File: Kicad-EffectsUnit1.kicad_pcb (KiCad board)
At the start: 2 copper layers, 100 x 100 mm, 161 parts, among them J101 In7, J102 Doepfer connector, J104 In6, J105 In3, J106 Out10, J107 Out11, J108 Out9, J109 Out6, J201 In, J202 Out, P201 HEADER_2x5_Doepfer, Q201 BC337, Q202 PZT2222A, Q203 PZT2222A, SW101 Dist 6, SW102 Crush A6, SW104 Rotary_Encoder_Switch, SW105 Dist 10, U101 TL072, U102 TL072, U201 TL072, U202 PT2399

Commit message: misc
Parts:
- removed C203, C204, C207, C208, C209: 100n, Capacitor_SMD:C_0805_2012Metric_Pad1.15x1.40mm_HandSolder
- removed C206: 100uF 16v, Capacitor_THT:CP_Radial_D5.0mm_P2.50mm
- removed D203: 1N1007, Diode_SMD:D_SOD-123
- removed U201: TL072, AJ-Dropbox-Kicad:AJ_SO-8_5.3x6.2mm_P1.27mm
- added C301: 100uF 16v, Capacitor_THT:CP_Radial_D5.0mm_P2.50mm, F.Cu at (228.7, 60.8)
- added C302: 100n, Capacitor_SMD:C_0805_2012Metric_Pad1.15x1.40mm_HandSolder, F.Cu at (209.9, 72.8)
- added C303: 100n, Capacitor_SMD:C_0805_2012Metric_Pad1.15x1.40mm_HandSolder, F.Cu at (221.7, 72.5)
- added C304: 100n, Capacitor_SMD:C_0805_2012Metric_Pad1.15x1.40mm_HandSolder, F.Cu at (232.8, 64.5)
- added C305: 100uF 16v, Capacitor_THT:CP_Radial_D5.0mm_P2.50mm, F.Cu at (221.4, 64.0)
- added C306: 100uF 16v, Capacitor_THT:CP_Radial_D5.0mm_P2.50mm, F.Cu at (215.8, 69.6)
- added C307: 100n, Capacitor_SMD:C_0805_2012Metric_Pad1.15x1.40mm_HandSolder, F.Cu at (226.5, 71.7)
- added C308: 100n, Capacitor_SMD:C_0805_2012Metric_Pad1.15x1.40mm_HandSolder, F.Cu at (231.2, 69.3)
- added C309: 100n, Capacitor_SMD:C_0805_2012Metric_Pad1.15x1.40mm_HandSolder, F.Cu at (232.8, 66.5)
- added C310: 100uF 16v, Capacitor_THT:CP_Radial_D5.0mm_P2.50mm, F.Cu at (215.8, 64.0)
- added D301: 1N1007, Diode_SMD:D_SOD-123, F.Cu at (227.0, 69.5)
- added D302: 1N1007, Diode_SMD:D_SOD-123, F.Cu at (222.2, 70.3)
- added D303: 1N1007, Diode_SMD:D_SOD-123, F.Cu at (222.2, 68.0)
- added D304: 5v6, Diode_SMD:D_MiniMELF_Handsoldering, F.Cu at (220.6, 59.6)
- added P301: HEADER_2x5_Doepfer, Connector_PinHeader_2.54mm:PinHeader_2x05_P2.54mm_Vertical, F.Cu at (209.8, 59.8)
- added Q301: BC337, Package_TO_SOT_THT:TO-92_Inline, F.Cu at (226.9, 66.3)
- added R301: 10k, Resistor_SMD:R_0805_2012Metric_Pad1.15x1.40mm_HandSolder, F.Cu at (230.2, 71.7)
- added R302: 0R, Resistor_SMD:R_0805_2012Metric_Pad1.15x1.40mm_HandSolder, F.Cu at (234.0, 71.3)
- C201, C202, C205, C210, C211, C212, C213, C214, C215, C216, C217, C218, C219, C220, C221, C222, C223, C224, C225, C226, D201, D202, D205, P201, Q201, Q202, Q203, R201, R202, R203, R204, R205, R206, R207, R208, R209, R210, R211, R212, R213, R214, R215, R216: moved to B.Cu
- D204: footprint Diode_SMD:D_MELF-RM10_Universal_Handsoldering -> Diode_SMD:D_MiniMELF_Handsoldering; moved to B.Cu
- moved J201 132.5 mm to (150.0, 145.0), turned to 270 degrees
- moved RV201 96.4 mm to (142.5, 128.5)
- moved U202 80.8 mm to (146.0, 94.0)
- moved RV202 65.0 mm to (142.5, 82.5)
- moved C210 62.1 mm to (155.0, 53.0)
- moved P201 57.6 mm to (148.8, 62.8)
- moved J202 47.4 mm to (150.0, 67.0), turned to 270 degrees
- moved C205 36.0 mm to (154.0, 72.0)
- moved D202 33.4 mm to (148.5, 10.4)
- moved D205 33.4 mm to (153.2, 10.4)
- moved R205 31.4 mm to (177.6, 11.5)
- moved Q201 31.0 mm to (171.7, 11.6)
- moved R207 28.8 mm to (181.4, 12.8)
- moved C222 27.6 mm to (177.6, 13.4)
- moved R206 25.1 mm to (181.4, 14.7)
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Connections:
- net -12Vb renamed Net-(P201-Pad1)
- C202 pad 2: +12Vb -> +5VA
- C222 pad 2: GND -> GNDA
- RV202 pad 3: GND -> GNDA
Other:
- outline, holes or cut-outs redrawn

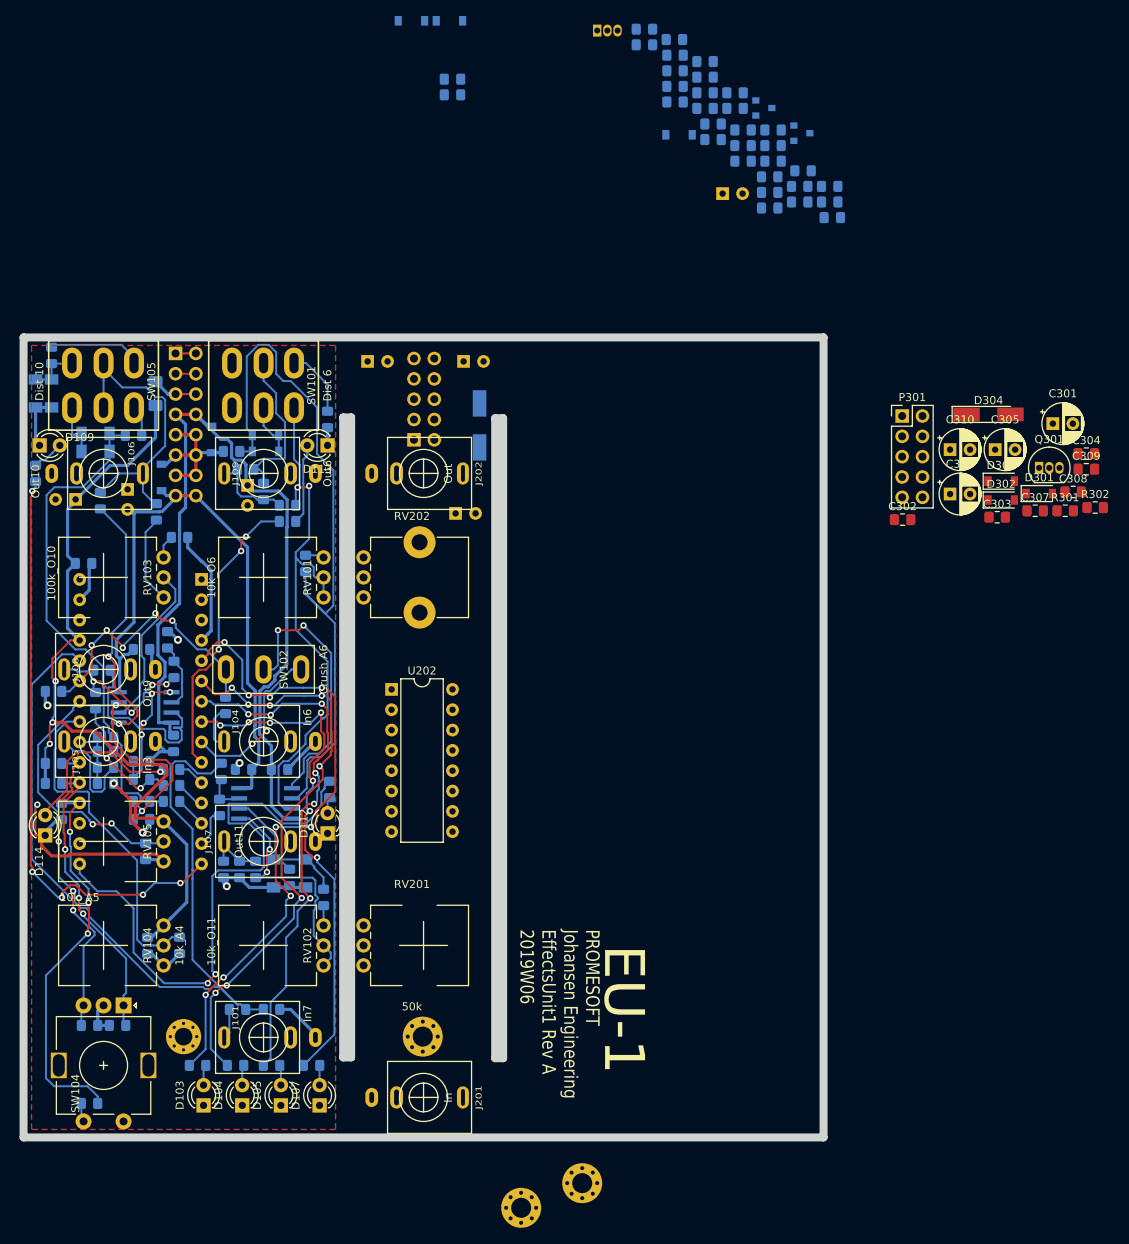
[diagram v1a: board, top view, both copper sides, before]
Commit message: Components placed on PT2399
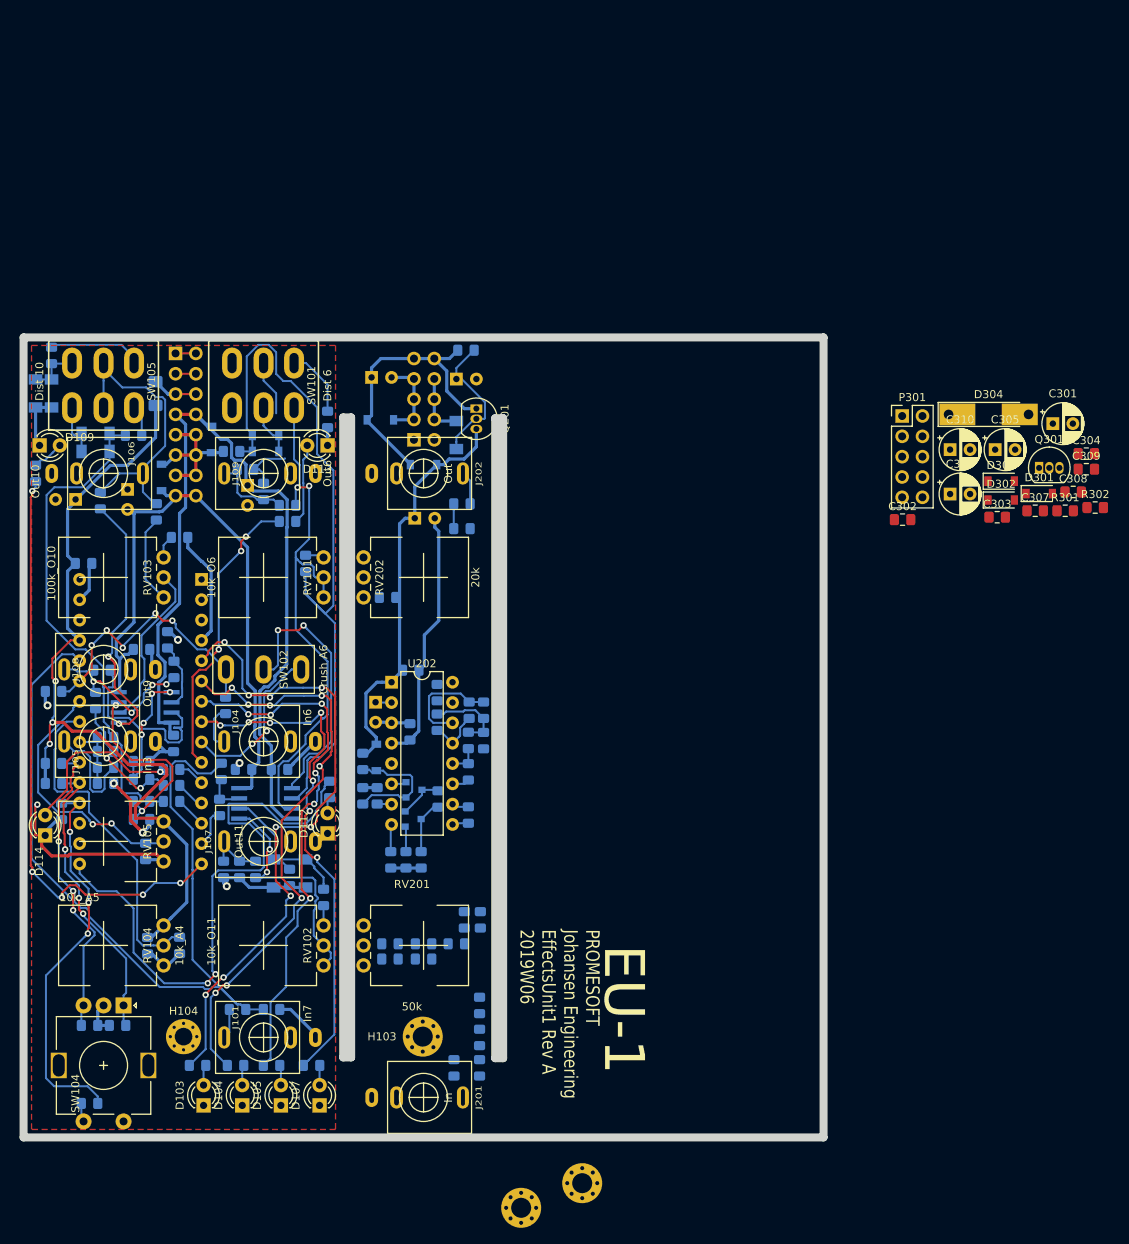
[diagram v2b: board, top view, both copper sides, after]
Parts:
- D204: footprint Diode_SMD:D_MiniMELF_Handsoldering -> Diode_SMD:D_MiniMELF
- D304: footprint Diode_SMD:D_MiniMELF_Handsoldering -> Diode_SMD:D_MELF-RM10_Universal_Handsoldering
- H103, H104, Q201: moved to F.Cu
- RV202: footprint Potentiometer_THT:Potentiometer_Alps_RK09K_Single_Vertical -> Potentiometer_THT:Potentiometer_China_RK09_Single_Vertical_AJ
- moved R204 125.9 mm to (153.8, 141.3), turned to 270 degrees
- moved C212 123.6 mm to (157.0, 141.3), turned to 270 degrees
- moved R203 119.5 mm to (157.0, 137.5), turned to 90 degrees
- moved R206 115.4 mm to (150.0, 125.8), turned to 180 degrees
- moved C211 113.9 mm to (157.0, 133.5), turned to 90 degrees
- moved R205 113.2 mm to (157.1, 122.8), turned to 90 degrees
- moved R207 113.1 mm to (155.1, 122.8), turned to 90 degrees
- moved R209 113.0 mm to (145.8, 125.8), turned to 180 degrees
- moved C218 110.5 mm to (150.0, 127.7)
- moved C217 110.1 mm to (145.8, 127.7), turned to 180 degrees
- moved R216 105.9 mm to (149.7, 115.3), turned to 90 degrees
- moved C222 100.3 mm to (142.4, 107.3), turned to 90 degrees
- moved C213 100.0 mm to (154.1, 125.8), turned to 180 degrees
- moved Q203 99.1 mm to (148.7, 110.2)
- moved C226 97.5 mm to (147.8, 115.3), turned to 90 degrees
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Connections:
- J201 pad S: GND -> GNDA
- J202 pad S: GND -> GNDA
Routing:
- net +5VA: track 0.00 -> 51.4 mm
- net GND: track 135.6 -> 185.9 mm
- net +12Vb: track 0.00 -> 35.6 mm
- net Net-(C210-Pad1): track 0.00 -> 17.3 mm
- net Net-(C222-Pad1): track 0.00 -> 15.0 mm
- net Net-(C219-Pad1): track 0.00 -> 13.4 mm
- net Net-(C221-Pad1): track 0.00 -> 10.1 mm
- net GNDA: track 0.00 -> 9.97 mm
- net Net-(Q203-Pad3): track 0.00 -> 6.79 mm
- net Net-(C219-Pad2): track 0.00 -> 6.54 mm
- net Net-(D110-Pad1): track 20.1 -> 14.0 mm
- net Net-(Q202-Pad3): track 0.00 -> 5.65 mm
- net Out: track 0.00 -> 4.32 mm
- net Net-(C220-Pad2): track 0.00 -> 3.86 mm
- net Net-(C225-Pad2): track 0.00 -> 3.44 mm
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
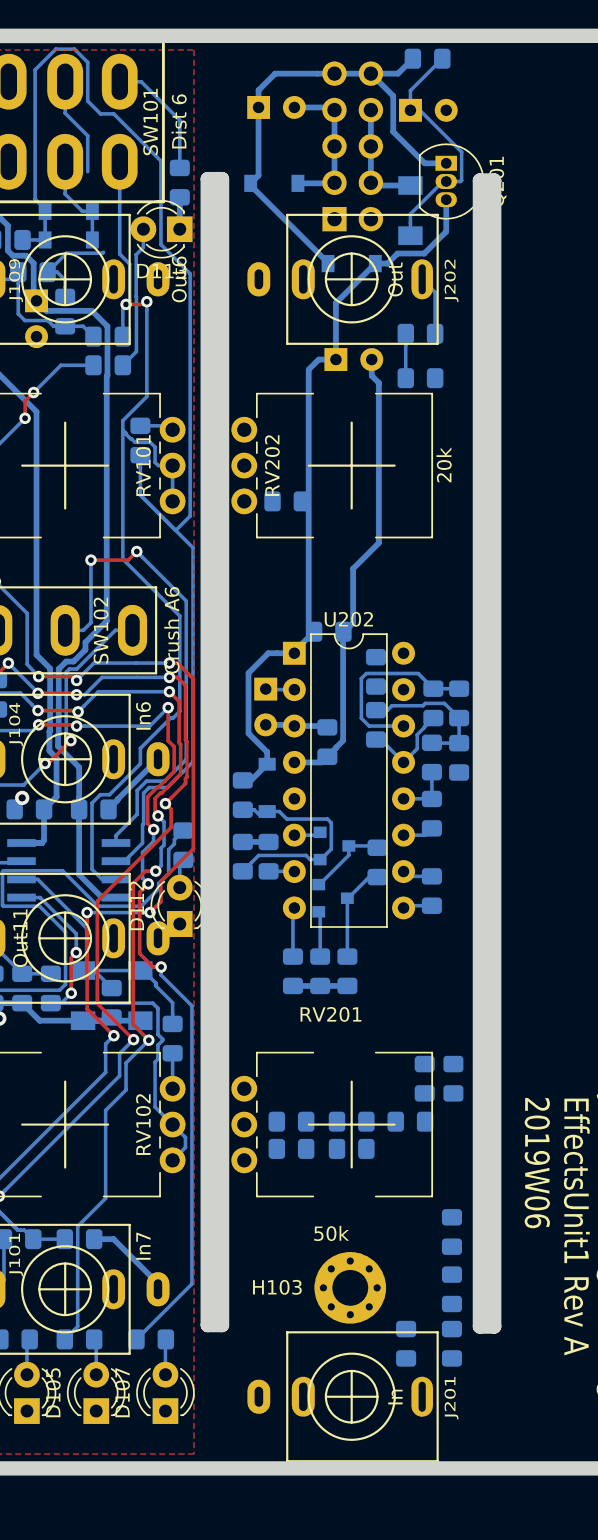
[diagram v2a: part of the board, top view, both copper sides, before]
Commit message: Added 78L05 reg
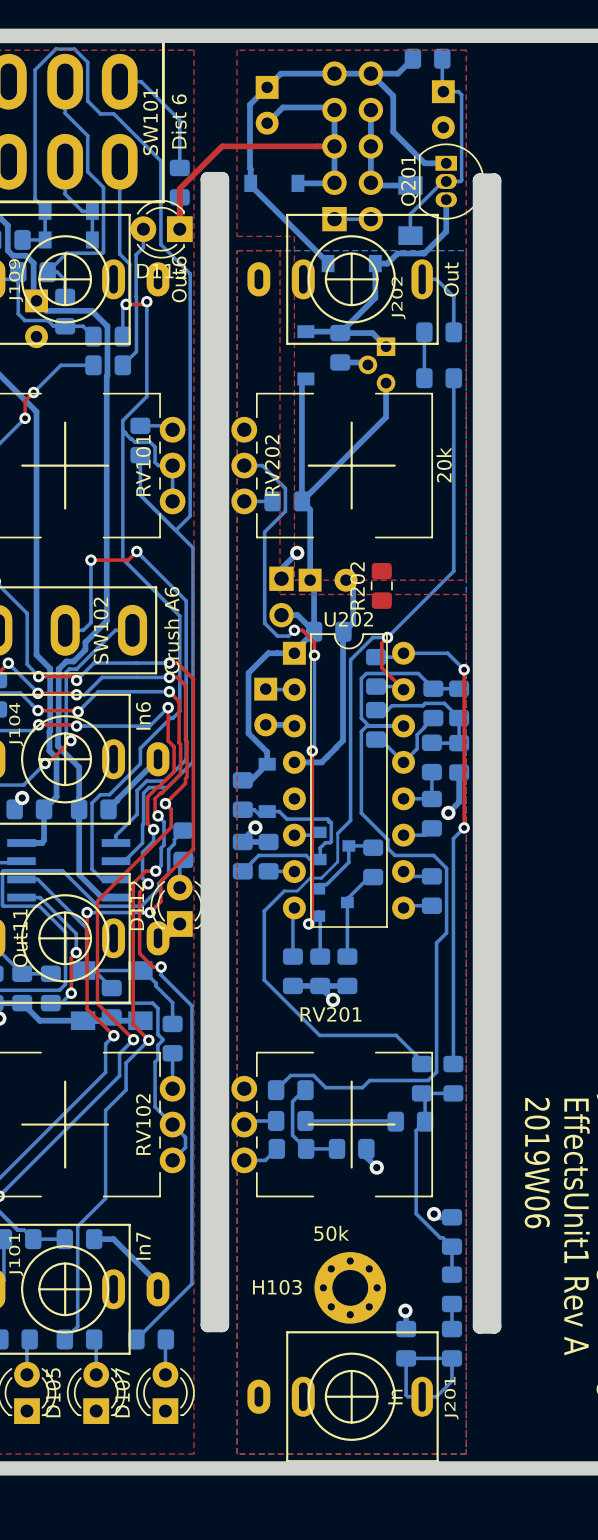
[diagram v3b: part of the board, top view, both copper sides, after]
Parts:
- added C203: 100n, Capacitor_SMD:C_0805_2012Metric_Pad1.15x1.40mm_HandSolder, B.Cu at (149.2, 71.8)
- added D203: 1N1007, Diode_SMD:D_SOD-123, B.Cu at (146.8, 72.3)
- added J203: Conn_01x02_Male, Connector_PinHeader_2.54mm:PinHeader_1x02_P2.54mm_Vertical, B.Cu at (145.1, 87.9)
- added U201: L7805, Package_TO_SOT_THT:TO-92, B.Cu at (152.4, 71.7)
- D204: value 5v6 -> 7v5
- R202: moved to F.Cu
- moved C205 15.5 mm to (147.1, 88.0)
- moved R202 11.5 mm to (152.1, 88.4), turned to 90 degrees
- moved R206 4.25 mm to (145.8, 125.8)
- moved C210 2.64 mm to (156.4, 53.9), turned to 270 degrees
- moved R209 2.20 mm to (145.8, 123.6)
- moved C201 1.52 mm to (144.1, 53.6), turned to 270 degrees
- moved C216 1.30 mm to (156.1, 70.7)
- moved R208 1.30 mm to (156.1, 73.9)
- moved R215 0.30 mm to (151.5, 107.7)
- moved Q203 0.30 mm to (148.7, 110.5)
- moved R207 0.20 mm to (154.9, 122.8)
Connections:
- D201 pad 2: +5VA -> +9V
- Q201 pad 3: +5VA -> +9V
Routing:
- net Net-(C214-Pad2): track 0.00 -> 69.1 mm, vias 0 -> 1
- net Net-(C219-Pad1): track 13.4 -> 57.0 mm
- net Net-(C226-Pad2): track 3.17 -> 42.0 mm, vias 0 -> 4
- net Net-(C214-Pad1): track 0.00 -> 34.6 mm, vias 0 -> 2
- net +9V: track 0.00 -> 20.0 mm
- net Net-(C211-Pad1): track 0.00 -> 16.1 mm
- net In: track 0.00 -> 11.0 mm
- net GNDA: track 9.97 -> 17.7 mm, vias 0 -> 6
- net Net-(C217-Pad1): track 0.00 -> 7.12 mm
- net Net-(C213-Pad2): track 0.00 -> 6.32 mm
- net Net-(D110-Pad1): track 14.0 -> 20.1 mm
- net GND: track 185.9 -> 191.2 mm, vias 7 -> 8
- net +5VA: track 51.4 -> 46.5 mm
- net Net-(C217-Pad2): track 0.00 -> 2.61 mm
- net Net-(P201-Pad1): track 0.00 -> 2.54 mm
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- added copper zone on B.Cu, net +5VA
- added copper zone on F.Cu, net GNDA

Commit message: PCB
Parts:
- C301, C302, C303, C304, C305, C306, C307, C308, C309, C310, D301, D302, D303, D304, P301, Q301, R301, R302: moved to B.Cu
- moved H101 99.7 mm to (169.9, 56.0)
- moved C302 57.3 mm to (168.9, 32.6)
- moved C303 56.9 mm to (180.8, 32.9)
- moved C307 55.8 mm to (185.5, 33.8)
- moved R301 55.8 mm to (189.3, 33.8)
- moved R302 55.2 mm to (193.0, 34.2)
- moved D302 54.0 mm to (181.3, 35.1)
- moved C306 53.0 mm to (174.9, 35.8)
- moved D301 53.0 mm to (186.0, 35.9)
- moved C308 52.7 mm to (190.3, 36.1)
- moved D303 51.1 mm to (181.3, 37.4)
- moved C309 49.3 mm to (191.9, 38.9)
- moved Q301 49.1 mm to (186.0, 39.1)
- moved C304 47.3 mm to (191.9, 40.9)
- moved C305 46.8 mm to (180.5, 41.4)
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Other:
- board text added: "Dist-Crush"
- board text added: "EU-2"
- board text added: "EffectsUnit1 Rev A"
- board text added: "PROMESOFT 2019W08 Johansen Engineering"
- board text added: "PROMESOFT Johansen Engineering EffectsUnit1 Rev A 2019W08"
- board text added: "Reverb"
- board text removed: "PROMESOFT Johansen Engineering EffectsUnit1 Rev A 2019W06"
